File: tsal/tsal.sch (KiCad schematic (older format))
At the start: 20 parts, among them J1 Indicator, J2 GLV, J3 TSAL, P1 TS+ (PreAIR), P2 TS-, P3 TS+ (PostAIR), Q1 Q_PMOS_GDS, U1 V7812W-500, U2 TL431, U3 TCMT1103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

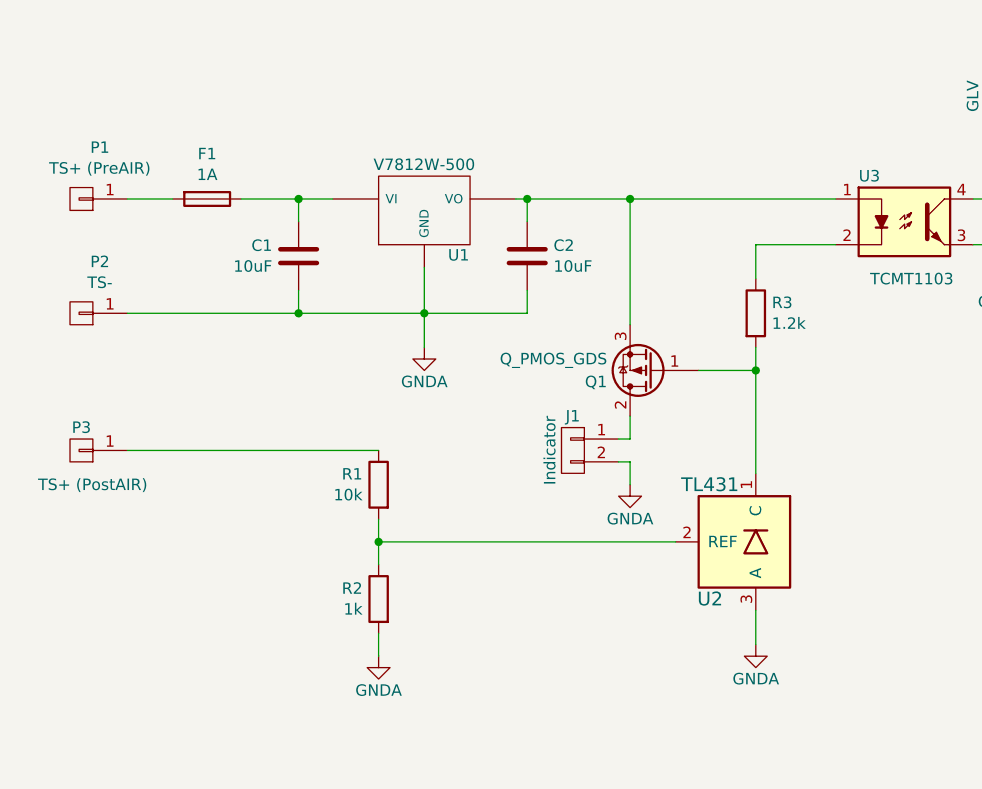
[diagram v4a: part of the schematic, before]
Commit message: Tweaks to IMD and tsal for ESF
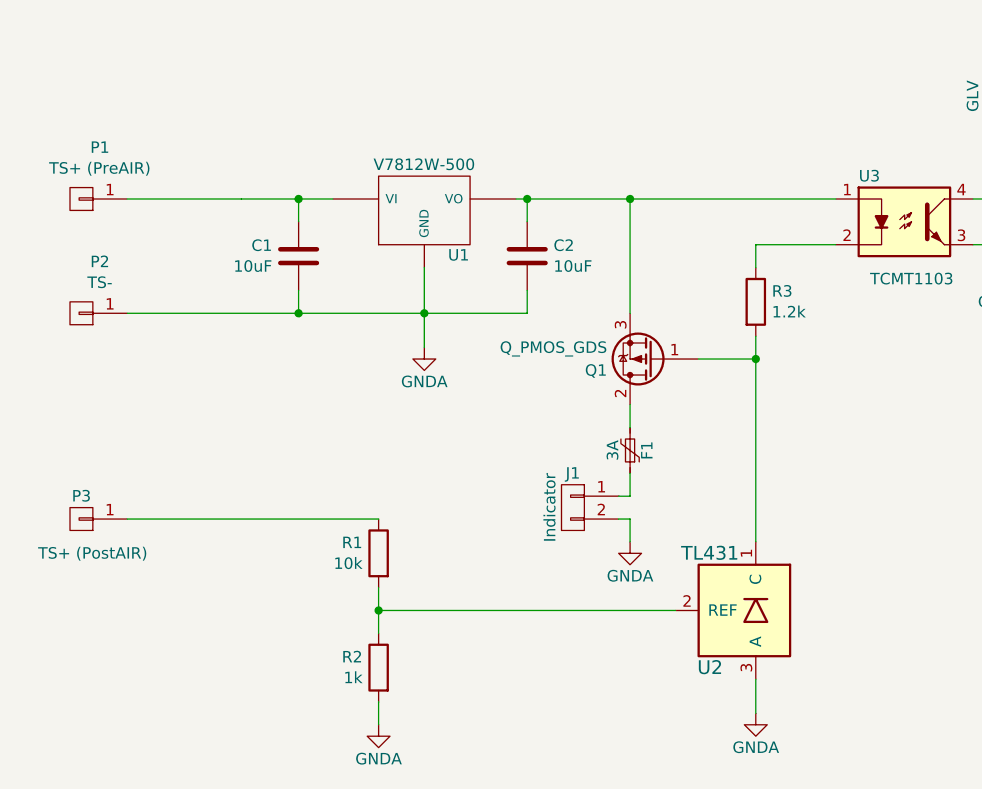
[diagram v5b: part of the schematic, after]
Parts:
- removed F1: 1A, Fuse_Holders_and_Fuses:Fuse_SMD1206_HandSoldering, symbol Fuse
- added F1: 3A, symbol Polyfuse_Small
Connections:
- net at C1.1, U1.1 (VI): now also P1.1 (P1)
- net at J1.1 (P1): now also F1.1; no longer Q1.2 (D)
- new net: F1.2, Q1.2 (D)
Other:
- moved on the sheet: J1, P3, Q1, R1, R2, R3, U2
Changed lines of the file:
@@
 L TL431 U2
 U 1 1 58CA1107
-P 5500 4000
-F 0 "U2" H 5700 3750 60  0000 C CNN
-F 1 "TL431" H 5700 4250 60  0000 C CNN
-F 2 "" H 5500 3950 60  0000 C CNN
-F 3 "" H 5500 3950 60  0000 C CNN
-	1    5500 4000
+P 5500 4300
+F 0 "U2" H 5700 4050 60  0000 C CNN
+F 1 "TL431" H 5700 4550 60  0000 C CNN
+F 2 "" H 5500 4250 60  0000 C CNN
+F 3 "" H 5500 4250 60  0000 C CNN
+	1    5500 4300
 	-1   0    0    -1
 $EndComp
@@
 L R R1
 U 1 1 58CA81E4
-P 3850 3750
-F 0 "R1" H 3920 3796 50  0000 L CNN
-F 1 "10k" H 3920 3705 50  0000 L CNN
-F 2 "Resistors_SMD:R_0805_HandSoldering" V 3780 3750 50  0001 C CNN
-F 3 "" H 3850 3750 50  0000 C CNN
-	1    3850 3750
+P 3850 4050
+F 0 "R1" H 3920 4096 50  0000 L CNN
+F 1 "10k" H 3920 4005 50  0000 L CNN
+F 2 "Resistors_SMD:R_0805_HandSoldering" V 3780 4050 50  0001 C CNN
+F 3 "" H 3850 4050 50  0000 C CNN
+	1    3850 4050
 	-1   0    0    -1
 $EndComp
@@
 L R R2
 U 1 1 58CA81EA
-P 3850 4250
-F 0 "R2" H 3920 4296 50  0000 L CNN
-F 1 "1k" H 3920 4205 50  0000 L CNN
-F 2 "Resistors_SMD:R_0805_HandSoldering" V 3780 4250 50  0001 C CNN
-F 3 "" H 3850 4250 50  0000 C CNN
-	1    3850 4250
+P 3850 4550
+F 0 "R2" H 3920 4596 50  0000 L CNN
+F 1 "1k" H 3920 4505 50  0000 L CNN
+F 2 "Resistors_SMD:R_0805_HandSoldering" V 3780 4550 50  0001 C CNN
+F 3 "" H 3850 4550 50  0000 C CNN
+	1    3850 4550
 	-1   0    0    -1
 $EndComp
@@
 L CONN_01X01 P3
 U 1 1 58CA81F6
-P 2550 3600
-F 0 "P3" H 2550 3500 50  0000 C CNN
-F 1 "TS+ (PostAIR)" H 2500 3750 50  0000 C CNN
-F 2 "Wire_Pads:SolderWirePad_single_1mmDrill" H 2550 3600 50  0001 C CNN
-F 3 "" H 2550 3600 50  0000 C CNN
-	1    2550 3600
+P 2550 3900
+F 0 "P3" H 2550 3800 50  0000 C CNN
+F 1 "TS+ (PostAIR)" H 2500 4050 50  0000 C CNN
+F 2 "Wire_Pads:SolderWirePad_single_1mmDrill" H 2550 3900 50  0001 C CNN
+F 3 "" H 2550 3900 50  0000 C CNN
+	1    2550 3900
 	-1   0    0    1
 $EndComp
@@
 $EndComp
 $Comp
-L Fuse F1
-U 1 1 58CACF32
-P 3100 2500
-F 0 "F1" V 2903 2500 50  0000 C CNN
-F 1 "1A" V 2994 2500 50  0000 C CNN
-F 2 "Fuse_Holders_and_Fuses:Fuse_SMD1206_HandSoldering" V 3030 2500 50  0001 C CNN
-F 3 "" H 3100 2500 50  0000 C CNN
-	1    3100 2500
-	0    1    1    0
-$EndComp
-$Comp
 L CONN_01X01 P1
 U 1 1 58CADA7B
@@
 L GNDA #PWR4
 U 1 1 58CAF931
-P 5500 4450
-F 0 "#PWR4" H 5500 4200 50  0001 C CNN
-F 1 "GNDA" H 5500 4300 50  0000 C CNN
-F 2 "" H 5500 4450 50  0001 C CNN
-F 3 "" H 5500 4450 50  0001 C CNN
-	1    5500 4450
+P 5500 4750
+F 0 "#PWR4" H 5500 4500 50  0001 C CNN
+F 1 "GNDA" H 5500 4600 50  0000 C CNN
+F 2 "" H 5500 4750 50  0001 C CNN
+F 3 "" H 5500 4750 50  0001 C CNN
+	1    5500 4750
 	1    0    0    -1
 $EndComp
@@
 L GNDA #PWR1
 U 1 1 58CAF999
-P 3850 4500
-F 0 "#PWR1" H 3850 4250 50  0001 C CNN
-F 1 "GNDA" H 3850 4350 50  0000 C CNN
-F 2 "" H 3850 4500 50  0001 C CNN
-F 3 "" H 3850 4500 50  0001 C CNN
-	1    3850 4500
+P 3850 4800
+F 0 "#PWR1" H 3850 4550 50  0001 C CNN
+F 1 "GNDA" H 3850 4650 50  0000 C CNN
+F 2 "" H 3850 4800 50  0001 C CNN
+F 3 "" H 3850 4800 50  0001 C CNN
+	1    3850 4800
 	1    0    0    -1
 $EndComp
@@
 L CONN_01X02 J1
 U 1 1 58CB2AB2
-P 4700 3600
-F 0 "J1" H 4700 3750 50  0000 C CNN
-F 1 "Indicator" V 4800 3600 50  0000 C CNN
-F 2 "" H 4700 3600 50  0001 C CNN
-F 3 "" H 4700 3600 50  0001 C CNN
-	1    4700 3600
+P 4700 3850
+F 0 "J1" H 4700 4000 50  0000 C CNN
+F 1 "Indicator" V 4800 3850 50  0000 C CNN
+F 2 "" H 4700 3850 50  0001 C CNN
+F 3 "" H 4700 3850 50  0001 C CNN
+	1    4700 3850
 	-1   0    0    -1
 $EndComp
@@
 L R R3
 U 1 1 58CB3E27
-P 5500 3000
-F 0 "R3" H 5570 3046 50  0000 L CNN
-F 1 "1.2k" H 5570 2955 50  0000 L CNN
-F 2 "Resistors_SMD:R_0805_HandSoldering" V 5430 3000 50  0001 C CNN
-F 3 "" H 5500 3000 50  0000 C CNN
-	1    5500 3000
+P 5500 2950
+F 0 "R3" H 5570 2996 50  0000 L CNN
+F 1 "1.2k" H 5570 2905 50  0000 L CNN
+F 2 "Resistors_SMD:R_0805_HandSoldering" V 5430 2950 50  0001 C CNN
+F 3 "" H 5500 2950 50  0000 C CNN
+	1    5500 2950
 	1    0    0    -1
 $EndComp
@@
 L Q_PMOS_GDS Q1
 U 1 1 58CBD40E
-P 5050 3250
-F 0 "Q1" H 5250 3300 50  0000 L CNN
-F 1 "Q_PMOS_GDS" H 5250 3200 50  0000 L CNN
-F 2 "" H 5250 3350 50  0001 C CNN
-F 3 "" H 5050 3250 50  0001 C CNN
-	1    5050 3250
+P 5050 3200
+F 0 "Q1" H 5250 3250 50  0000 L CNN
+F 1 "Q_PMOS_GDS" H 5250 3150 50  0000 L CNN
+F 2 "" H 5250 3300 50  0001 C CNN
+F 3 "" H 5050 3200 50  0001 C CNN
+	1    5050 3200
 	-1   0    0    1
 $EndComp
@@
 	-1   0    0    -1
 $EndComp
+$Comp
+L GNDA #PWR3
+U 1 1 58CC0EB2
+P 4950 4000
+F 0 "#PWR3" H 4950 3750 50  0001 C CNN
+F 1 "GNDA" H 4950 3850 50  0000 C CNN
+F 2 "" H 4950 4000 50  0001 C CNN
+F 3 "" H 4950 4000 50  0001 C CNN
+	1    4950 4000
+	1    0    0    -1
+$EndComp
+$Comp
+L Polyfuse_Small F1
+U 1 1 58D72905
+P 4950 3600
+F 0 "F1" V 4875 3600 50  0000 C CNN
+F 1 "3A" V 5025 3600 50  0000 C CNN
+F 2 "" H 5000 3400 50  0001 L CNN
+F 3 "" H 4950 3600 50  0001 C CNN
+	1    4950 3600
+	-1   0    0    1
+$EndComp
 Wire Wire Line
 	6750 2100 6900 2100
@@
 Wire Wire Line
 	6750 2000 6850 2000
-Connection ~ 5500 3250
-Wire Wire Line
-	5500 3150 5500 3250
-Wire Wire Line
-	5500 3250 5500 3700
+Connection ~ 5500 3200
+Wire Wire Line
+	5500 3100 5500 3200
 Wire Wire Line
 	8350 2400 8500 2400
@@
 	8000 2400 8150 2400
 Wire Wire Line
-	5500 2700 5500 2850
+	5500 2700 5500 2800
 Connection ~ 3500 3000
 Wire Wire Line
-	2750 2500 2950 2500
+	2750 2500 3250 2500
 Connection ~ 3500 2500
 Wire Wire Line
@@
 	6850 2500 7100 2500
 Wire Wire Line
-	3850 3600 2750 3600
-Wire Wire Line
-	3850 3900 3850 4000
-Wire Wire Line
-	3850 4000 3850 4100
-Wire Wire Line
-	3850 4500 3850 4400
-Wire Wire Line
-	3850 4000 5150 4000
-Connection ~ 3850 4000
+	3850 3900 2750 3900
+Wire Wire Line
+	3850 4200 3850 4300
+Wire Wire Line
+	3850 4300 3850 4400
+Wire Wire Line
+	3850 4800 3850 4700
+Wire Wire Line
+	3850 4300 5150 4300
+Connection ~ 3850 4300
 Wire Wire Line
 	6900 2400 7100 2400
@@
 	7000 2700 7000 2600
 Wire Wire Line
-	5500 4450 5500 4300
+	5500 4750 5500 4600
 Connection ~ 8000 2400
 Wire Wire Line
@@
 	8400 2650 8400 2500
 Wire Wire Line
-	5250 3250 5500 3250
-Wire Wire Line
-	4950 3050 4950 2500
+	5250 3200 5500 3200
+Wire Wire Line
+	4950 3000 4950 2500
 Connection ~ 4950 2500
 Wire Wire Line
-	4900 3550 4950 3550
-Wire Wire Line
-	4950 3550 4950 3450
-$Comp
-L GNDA #PWR3
-U 1 1 58CC0EB2
-P 4950 3750
-F 0 "#PWR3" H 4950 3500 50  0001 C CNN
-F 1 "GNDA" H 4950 3600 50  0000 C CNN
-F 2 "" H 4950 3750 50  0001 C CNN
-F 3 "" H 4950 3750 50  0001 C CNN
-	1    4950 3750
-	1    0    0    -1
-$EndComp
-Wire Wire Line
-	4900 3650 4950 3650
-Wire Wire Line
-	4950 3650 4950 3750
+	4900 3800 4950 3800
+Wire Wire Line
+	4900 3900 4950 3900
+Wire Wire Line
+	4950 3900 4950 4000
+Wire Wire Line
+	4950 3500 4950 3400
+Wire Wire Line
+	4950 3800 4950 3700
+Wire Wire Line
+	5500 3200 5500 4000
 $EndSCHEMATC

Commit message: TSAL board layout
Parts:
- removed Q1: Q_PMOS_GDS, symbol Q_PMOS_GDS
- added MK1, MK3: Mounting_Hole, Mounting_Holes:MountingHole_3mm, symbol Mounting_Hole
- added Q1: Q_PMOS_GSD, UNCAMotorsports:SOT23-3, symbol Q_PMOS_GSD
- C1, C2: footprint Capacitors_ThroughHole:CP_Radial_D5.0mm_P2.00mm -> Capacitors_SMD:C_0805_HandSoldering
- F1, F2: footprint (none) -> SMD_Packages:SMD-1210_Pol
- J1, J2, J3: footprint (none) -> Pin_Headers:Pin_Header_Straight_1x02
- P1, P2: footprint Wire_Pads:SolderWirePad_single_2mmDrill -> Wire_Pads:SolderWirePad_single_1mmDrill
- U1: footprint (none) -> UNCAMotorsports:V78W-500
- U2: footprint (none) -> UNCAMotorsports:SOT23-3
- U4: footprint (none) -> UNCAMotorsports:TO-252-5
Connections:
- net at R3.2, U2.1 (C): now also Q1.1 (G)
- net at C2.1, U1.3 (VO), U3.1: now also Q1.2 (S)
- net at F1.2: now also Q1.3 (D)
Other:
- note added: "2mm gap"
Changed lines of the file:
@@
 LIBS:valves
 LIBS:UNCAMotorsports
+LIBS:mechanical
 LIBS:tsal-cache
 EELAYER 25 0
@@
 F 0 "J3" H 8700 2600 50  0000 C CNN
 F 1 "TSAL" V 8800 2450 50  0000 C CNN
-F 2 "" H 8700 2450 50  0001 C CNN
+F 2 "Pin_Headers:Pin_Header_Straight_1x02" H 8700 2450 50  0001 C CNN
 F 3 "" H 8700 2450 50  0001 C CNN
 	1    8700 2450
@@
 $EndComp
 $Comp
-L GND #PWR8
+L GND #PWR01
 U 1 1 58CA0A4F
 P 8400 2650
-F 0 "#PWR8" H 8400 2400 50  0001 C CNN
+F 0 "#PWR01" H 8400 2400 50  0001 C CNN
 F 1 "GND" H 8400 2500 50  0000 C CNN
 F 2 "" H 8400 2650 50  0001 C CNN
@@
 F 0 "U4" H 7300 2750 60  0000 C CNN
 F 1 "BTS6133D" H 7550 2250 60  0000 C CNN
-F 2 "" H 7650 2700 60  0000 C CNN
+F 2 "UNCAMotorsports:TO-252-5" H 7650 2700 60  0001 C CNN
 F 3 "" H 7650 2700 60  0000 C CNN
 	1    7500 2500
@@
 F 0 "U2" H 5700 4050 60  0000 C CNN
 F 1 "TL431" H 5700 4550 60  0000 C CNN
-F 2 "" H 5500 4250 60  0000 C CNN
+F 2 "UNCAMotorsports:SOT23-3" H 5500 4250 60  0001 C CNN
 F 3 "" H 5500 4250 60  0000 C CNN
 	1    5500 4300
@@
 $EndComp
 $Comp
-L GND #PWR7
+L GND #PWR02
 U 1 1 58CA651D
 P 7000 3100
-F 0 "#PWR7" H 7000 2850 50  0001 C CNN
+F 0 "#PWR02" H 7000 2850 50  0001 C CNN
 F 1 "GND" H 7000 2950 50  0000 C CNN
 F 2 "" H 7000 3100 50  0001 C CNN
@@
 $EndComp
 $Comp
-L +12V #PWR6
+L +12V #PWR03
 U 1 1 58CA675E
 P 6850 1900
-F 0 "#PWR6" H 6850 1750 50  0001 C CNN
+F 0 "#PWR03" H 6850 1750 50  0001 C CNN
 F 1 "+12V" H 6850 2040 50  0000 C CNN
 F 2 "" H 6850 1900 50  0001 C CNN
@@
 $EndComp
 $Comp
-L GND #PWR5
+L GND #PWR04
 U 1 1 58CA8F7F
 P 6550 2800
-F 0 "#PWR5" H 6550 2550 50  0001 C CNN
+F 0 "#PWR04" H 6550 2550 50  0001 C CNN
 F 1 "GND" H 6550 2650 50  0000 C CNN
 F 2 "" H 6550 2800 50  0001 C CNN
@@
 F 0 "U1" H 4200 2354 50  0000 C CNN
 F 1 "V7812W-500" H 4050 2750 50  0000 C CNN
-F 2 "" H 4050 2550 50  0000 C CNN
+F 2 "UNCAMotorsports:V78W-500" H 4050 2550 50  0001 C CNN
 F 3 "" H 4050 2550 50  0000 C CNN
 	1    4050 2550
@@
 F 0 "C2" H 4615 2796 50  0000 L CNN
 F 1 "10uF" H 4615 2705 50  0000 L CNN
-F 2 "Capacitors_ThroughHole:CP_Radial_D5.0mm_P2.00mm" H 4538 2600 50  0001 C CNN
+F 2 "Capacitors_SMD:C_0805_HandSoldering" H 4538 2600 50  0001 C CNN
 F 3 "" H 4500 2750 50  0000 C CNN
 	1    4500 2750
@@
 F 0 "C1" H 3615 2796 50  0000 L CNN
 F 1 "10uF" H 3615 2705 50  0000 L CNN
-F 2 "Capacitors_ThroughHole:CP_Radial_D5.0mm_P2.00mm" H 3538 2600 50  0001 C CNN
+F 2 "Capacitors_SMD:C_0805_HandSoldering" H 3538 2600 50  0001 C CNN
 F 3 "" H 3500 2750 50  0000 C CNN
 	1    3500 2750
@@
 F 0 "P1" H 2469 2275 50  0000 C CNN
 F 1 "TS+ (PreAIR)" H 2469 2366 50  0000 C CNN
-F 2 "Wire_Pads:SolderWirePad_single_2mmDrill" H 2550 2500 50  0001 C CNN
+F 2 "Wire_Pads:SolderWirePad_single_1mmDrill" H 2550 2500 50  0001 C CNN
 F 3 "" H 2550 2500 50  0000 C CNN
 	1    2550 2500
@@
 F 0 "P2" H 2469 2775 50  0000 C CNN
 F 1 "TS-" H 2469 2866 50  0000 C CNN
-F 2 "Wire_Pads:SolderWirePad_single_2mmDrill" H 2550 3000 50  0001 C CNN
+F 2 "Wire_Pads:SolderWirePad_single_1mmDrill" H 2550 3000 50  0001 C CNN
 F 3 "" H 2550 3000 50  0000 C CNN
 	1    2550 3000
@@
 $EndComp
 $Comp
-L GNDA #PWR2
+L GNDA #PWR05
 U 1 1 58CAF851
 P 4050 3150
-F 0 "#PWR2" H 4050 2900 50  0001 C CNN
+F 0 "#PWR05" H 4050 2900 50  0001 C CNN
 F 1 "GNDA" H 4050 3000 50  0000 C CNN
 F 2 "" H 4050 3150 50  0001 C CNN
@@
 $EndComp
 $Comp
-L GNDA #PWR4
+L GNDA #PWR06
 U 1 1 58CAF931
 P 5500 4750
-F 0 "#PWR4" H 5500 4500 50  0001 C CNN
+F 0 "#PWR06" H 5500 4500 50  0001 C CNN
 F 1 "GNDA" H 5500 4600 50  0000 C CNN
 F 2 "" H 5500 4750 50  0001 C CNN
@@
 $EndComp
 $Comp
-L GNDA #PWR1
+L GNDA #PWR07
 U 1 1 58CAF999
 P 3850 4800
-F 0 "#PWR1" H 3850 4550 50  0001 C CNN
+F 0 "#PWR07" H 3850 4550 50  0001 C CNN
 F 1 "GNDA" H 3850 4650 50  0000 C CNN
 F 2 "" H 3850 4800 50  0001 C CNN
@@
 F 0 "J1" H 4700 4000 50  0000 C CNN
 F 1 "Indicator" V 4800 3850 50  0000 C CNN
-F 2 "" H 4700 3850 50  0001 C CNN
+F 2 "Pin_Headers:Pin_Header_Straight_1x02" H 4700 3850 50  0001 C CNN
 F 3 "" H 4700 3850 50  0001 C CNN
 	1    4700 3850
@@
 F 0 "F2" V 8175 2400 50  0000 C CNN
 F 1 "3A" V 8325 2400 50  0000 C CNN
-F 2 "" H 8300 2200 50  0001 L CNN
+F 2 "SMD_Packages:SMD-1210_Pol" H 8300 2200 50  0001 L CNN
 F 3 "" H 8250 2400 50  0001 C CNN
 	1    8250 2400
 	0    1    1    0
-$EndComp
-$Comp
-L Q_PMOS_GDS Q1
-U 1 1 58CBD40E
-P 5050 3200
-F 0 "Q1" H 5250 3250 50  0000 L CNN
-F 1 "Q_PMOS_GDS" H 5250 3150 50  0000 L CNN
-F 2 "" H 5250 3300 50  0001 C CNN
-F 3 "" H 5050 3200 50  0001 C CNN
-	1    5050 3200
-	-1   0    0    1
 $EndComp
 $Comp
@@
 F 0 "J2" H 6550 2200 50  0000 C CNN
 F 1 "GLV" V 6650 2050 50  0000 C CNN
-F 2 "" H 6550 2050 50  0001 C CNN
+F 2 "Pin_Headers:Pin_Header_Straight_1x02" H 6550 2050 50  0001 C CNN
 F 3 "" H 6550 2050 50  0001 C CNN
 	1    6550 2050
@@
 $EndComp
 $Comp
-L GNDA #PWR3
+L GNDA #PWR08
 U 1 1 58CC0EB2
 P 4950 4000
-F 0 "#PWR3" H 4950 3750 50  0001 C CNN
+F 0 "#PWR08" H 4950 3750 50  0001 C CNN
 F 1 "GNDA" H 4950 3850 50  0000 C CNN
 F 2 "" H 4950 4000 50  0001 C CNN
@@
 F 0 "F1" V 4875 3600 50  0000 C CNN
 F 1 "3A" V 5025 3600 50  0000 C CNN
-F 2 "" H 5000 3400 50  0001 L CNN
+F 2 "SMD_Packages:SMD-1210_Pol" H 5000 3400 50  0001 L CNN
 F 3 "" H 4950 3600 50  0001 C CNN
 	1    4950 3600
@@
 	6850 2000 6850 1900
 Wire Wire Line
-	6750 2000 6850 2000
+	6750 2000 7250 2000
 Connection ~ 5500 3200
 Wire Wire Line
-	5500 3100 5500 3200
+	5500 3100 5500 4000
 Wire Wire Line
 	8350 2400 8500 2400
 Wire Wire Line
-	7900 2400 8000 2400
-Wire Wire Line
-	8000 2400 8150 2400
+	7900 2400 8150 2400
 Wire Wire Line
 	5500 2700 5500 2800
 Connection ~ 3500 3000
 Wire Wire Line
-	2750 2500 3250 2500
+	2750 2500 3650 2500
 Connection ~ 3500 2500
-Wire Wire Line
-	3250 2500 3500 2500
-Wire Wire Line
-	3500 2500 3650 2500
 Wire Wire Line
 	3500 2600 3500 2500
@@
 Connection ~ 4050 3000
 Wire Wire Line
-	2750 3000 3500 3000
-Wire Wire Line
-	3500 3000 4050 3000
-Wire Wire Line
-	4050 3000 4500 3000
+	2750 3000 4500 3000
 Wire Wire Line
 	4500 3000 4500 2900
@@
 	4500 2600 4500 2500
 Wire Wire Line
-	4050 2800 4050 3000
-Wire Wire Line
-	4050 3000 4050 3150
-Wire Wire Line
-	4450 2500 4500 2500
-Wire Wire Line
-	4500 2500 4950 2500
-Wire Wire Line
-	4950 2500 5850 2500
+	4050 2800 4050 3150
+Wire Wire Line
+	4450 2500 5850 2500
 Wire Wire Line
 	6550 2700 6550 2800
@@
 	3850 3900 2750 3900
 Wire Wire Line
-	3850 4200 3850 4300
-Wire Wire Line
-	3850 4300 3850 4400
+	3850 4200 3850 4400
 Wire Wire Line
 	3850 4800 3850 4700
@@
 	8400 2650 8400 2500
 Wire Wire Line
-	5250 3200 5500 3200
+	5500 3200 5250 3200
 Wire Wire Line
 	4950 3000 4950 2500
@@
 Wire Wire Line
 	4950 3800 4950 3700
-Wire Wire Line
-	5500 3200 5500 4000
+$Comp
+L PWR_FLAG #FLG09
+U 1 1 5913E334
+P 2400 5100
+F 0 "#FLG09" H 2400 5175 50  0001 C CNN
+F 1 "PWR_FLAG" H 2400 5250 50  0000 C CNN
+F 2 "" H 2400 5100 50  0001 C CNN
+F 3 "" H 2400 5100 50  0001 C CNN
+	1    2400 5100
+	1    0    0    -1
+$EndComp
+$Comp
+L GNDA #PWR010
+U 1 1 5913E382
+P 2400 5250
+F 0 "#PWR010" H 2400 5000 50  0001 C CNN
+F 1 "GNDA" H 2400 5100 50  0000 C CNN
+F 2 "" H 2400 5250 50  0001 C CNN
+F 3 "" H 2400 5250 50  0001 C CNN
+	1    2400 5250
+	1    0    0    -1
+$EndComp
+Wire Wire Line
+	2400 5250 2400 5100
+$Comp
+L GND #PWR011
+U 1 1 5913E578
+P 2850 5250
+F 0 "#PWR011" H 2850 5000 50  0001 C CNN
+F 1 "GND" H 2850 5100 50  0000 C CNN
+F 2 "" H 2850 5250 50  0001 C CNN
+F 3 "" H 2850 5250 50  0001 C CNN
+	1    2850 5250
+	1    0    0    -1
+$EndComp
+$Comp
+L PWR_FLAG #FLG012
+U 1 1 5913E763
+P 2850 5100
+F 0 "#FLG012" H 2850 5175 50  0001 C CNN
+F 1 "PWR_FLAG" H 2850 5250 50  0000 C CNN
+F 2 "" H 2850 5100 50  0001 C CNN
+F 3 "" H 2850 5100 50  0001 C CNN
+	1    2850 5100
+	1    0    0    -1
+$EndComp
+Wire Wire Line
+	2850 5100 2850 5250
+$Comp
+L PWR_FLAG #FLG013
+U 1 1 5913EA22
+P 7250 1850
+F 0 "#FLG013" H 7250 1925 50  0001 C CNN
+F 1 "PWR_FLAG" H 7250 2000 50  0000 C CNN
+F 2 "" H 7250 1850 50  0001 C CNN
+F 3 "" H 7250 1850 50  0001 C CNN
+	1    7250 1850
+	1    0    0    -1
+$EndComp
+Wire Wire Line
+	7250 2000 7250 1850
+Connection ~ 6850 2000
+$Comp
+L Q_PMOS_GSD Q1
+U 1 1 59140726
+P 5050 3200
+F 0 "Q1" H 5250 3250 50  0000 L CNN
+F 1 "Q_PMOS_GSD" H 5250 3150 50  0000 L CNN
+F 2 "UNCAMotorsports:SOT23-3" H 5250 3300 50  0001 C CNN
+F 3 "" H 5050 3200 50  0001 C CNN
+	1    5050 3200
+	-1   0    0    1
+$EndComp
+$Comp
+L Mounting_Hole MK1
+U 1 1 59147268
+P 7200 5950
+F 0 "MK1" H 7200 6150 50  0000 C CNN
+F 1 "Mounting_Hole" H 7200 6075 50  0000 C CNN
+F 2 "Mounting_Holes:MountingHole_3mm" H 7200 5950 50  0001 C CNN
+F 3 "" H 7200 5950 50  0001 C CNN
+	1    7200 5950
+	1    0    0    -1
+$EndComp
+$Comp
+L Mounting_Hole MK3
+U 1 1 59147621
+P 7550 5950
+F 0 "MK3" H 7550 6150 50  0000 C CNN
+F 1 "Mounting_Hole" H 7550 6075 50  0000 C CNN
+F 2 "Mounting_Holes:MountingHole_3mm" H 7550 5950 50  0001 C CNN
+F 3 "" H 7550 5950 50  0001 C CNN
+	1    7550 5950
+	1    0    0    -1
+$EndComp
+Wire Notes Line
+	6200 1800 6200 3350
+Text Notes 6000 3450 0    60   ~ 0
+2mm gap
 $EndSCHEMATC
